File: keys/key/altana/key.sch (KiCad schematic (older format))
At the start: 13 parts

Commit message: Update
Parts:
- removed J? (x10): Conn_01x01_Female, Connector_Pin:Pin_D1.1mm_L8.5mm_W2.5mm_FlatFork, symbol Connector:Conn_01x01_Female
- added J1, J7: (+), kbd:wirepad-h0.8mm-d1.8mm, symbol Connector:Conn_01x01_Female
- added J10, J4: R, kbd:wirepad-h0.8mm-d1.8mm, symbol Connector:Conn_01x01_Female
- added J11, J5: DI, kbd:wirepad-h0.8mm-d1.8mm, symbol Connector:Conn_01x01_Female
- added J12, J6: DO, kbd:wirepad-h0.8mm-d1.8mm, symbol Connector:Conn_01x01_Female
- added J2, J8: (-), kbd:wirepad-h0.8mm-d1.8mm, symbol Connector:Conn_01x01_Female
- added J3, J9: C, kbd:wirepad-h0.8mm-d1.8mm, symbol Connector:Conn_01x01_Female
- D1: renamed from D?; footprint keebio_parts:Diode-Hybrid-Back -> footprint:diode
- gave numbers to parts that had none: 2
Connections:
- net GND: now also J2.1 (Pin_1), J8.1 (Pin_1)
- net VCC: now also J1.1 (Pin_1), J7.1 (Pin_1)
- net LED_DO: now reaches L1.1 (DOUT)
- net LED_DO: now also J12.1 (Pin_1), J6.1 (Pin_1)
- net LED_DI: now reaches L1.3 (DIN)
- net LED_DI: now also J11.1 (Pin_1), J5.1 (Pin_1)
- net COL renamed COL_N
- net COL_N: now also J3.1 (Pin_1), J9.1 (Pin_1)
- net ROW renamed ROW_N
- net ROW_N: now also J10.1 (Pin_1), J4.1 (Pin_1)
- no-connect marks 2 -> 0
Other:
- note added: "CONNECTORS"
- note added: "RGB LED"
- note added: "SWITCH"
- moved on the sheet: D1, L1, SW1

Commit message: Update project using kicad symbols whenever is possible and also update footprints to use project's library
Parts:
- removed L1: SK6812MINI, kbd:SK6812MINI_rev, symbol kbd:SK6812MINI
- added D2: SK6812MINI, Altana:SK6812MINI, symbol Altana:SK6812MINI
- D1: value D -> 1N4148; footprint footprint:diode -> Altana:diode
- J1, J10, J11, J12, J2, J3, J4, J5, J6, J7, J8, J9: footprint kbd:wirepad-h0.8mm-d1.8mm -> Altana:wirepad
- SW1: footprint kbd:MX_Hotswap_single -> Altana:Switch_MX_Hotswap
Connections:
- net GND: now also D2.2 (VSS)
- net LED_DI: now also D2.3 (DIN)
- net LED_DO: now also D2.1 (DOUT)
- net VCC: now also D2.4 (VDD)
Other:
- note removed: "CONNECTORS"
- note removed: "RGB LED"
- note removed: "SWITCH"
- moved on the sheet: D1
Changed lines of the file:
@@
 L Device:D D?
 U 1 1 5F6D17DD
-P 5300 3250
+P 5875 2875
 AR Path="/5F6D17DD" Ref="D?"  Part="1"
 AR Path="/5F6CE726/5F6D17DD" Ref="D1"  Part="1"
 AR Path="/5F6DC527/5F6D17DD" Ref="D?"  Part="1"
 AR Path="/5F6DC5E9/5F6D17DD" Ref="D?"  Part="1"
-F 0 "D1" H 5325 3050 50  0000 R CNN
-F 1 "D" H 5300 3150 50  0000 R CNN
-F 2 "footprint:diode" H 5300 3250 50  0001 C CNN
-F 3 "~" H 5300 3250 50  0001 C CNN
-	1    5300 3250
+F 0 "D1" H 5925 2650 50  0000 R CNN
+F 1 "1N4148" H 6025 2750 50  0000 R CNN
+F 2 "Altana:diode" H 5875 2875 50  0001 C CNN
+F 3 "~" H 5875 2875 50  0001 C CNN
+	1    5875 2875
 	-1   0    0    1
 $EndComp
-$Comp
-L kbd:SK6812MINI L?
-U 1 1 5F6D17E3
-P 6700 3150
-AR Path="/5F6D17E3" Ref="L?"  Part="1"
-AR Path="/5F6CE726/5F6D17E3" Ref="L1"  Part="1"
-AR Path="/5F6DC527/5F6D17E3" Ref="L?"  Part="1"
-AR Path="/5F6DC5E9/5F6D17E3" Ref="L?"  Part="1"
-F 0 "L1" H 6700 3350 51  0000 C CNN
-F 1 "SK6812MINI" H 6700 3150 16  0000 C CNN
-F 2 "kbd:SK6812MINI_rev" H 6700 3150 60  0001 C CNN
-F 3 "" H 6700 3150 60  0001 C CNN
-	1    6700 3150
-	-1   0    0    -1
-$EndComp
-$Comp
-L Switch:SW_Push SW?
-U 1 1 5F6D180E
-P 4900 3250
-AR Path="/5F6D180E" Ref="SW?"  Part="1"
-AR Path="/5F6CE726/5F6D180E" Ref="SW1"  Part="1"
-AR Path="/5F6DC527/5F6D180E" Ref="SW?"  Part="1"
-AR Path="/5F6DC5E9/5F6D180E" Ref="SW?"  Part="1"
-F 0 "SW1" H 4900 3535 50  0000 C CNN
-F 1 "SW_Push" H 4900 3444 50  0000 C CNN
-F 2 "kbd:MX_Hotswap_single" H 4900 3450 50  0001 C CNN
-F 3 "~" H 4900 3450 50  0001 C CNN
-	1    4900 3250
-	1    0    0    -1
-$EndComp
-Text HLabel 4600 3250 0    50   BiDi ~ 0
+Text HLabel 5150 2875 0    50   BiDi ~ 0
 COL_N
-Text HLabel 5500 3250 2    50   BiDi ~ 0
+Text HLabel 6075 2875 2    50   BiDi ~ 0
 ROW_N
 Wire Wire Line
-	5100 3250 5150 3250
-Wire Wire Line
-	5450 3250 5500 3250
-Wire Wire Line
-	4600 3250 4700 3250
-Wire Wire Line
-	6900 3250 6975 3250
-Text Notes 4700 2575 0    89   ~ 0
-SWITCH
-Text Notes 6450 2600 0    89   ~ 0
-RGB LED
+	5650 2875 5725 2875
+Wire Wire Line
+	6025 2875 6075 2875
+Wire Wire Line
+	5150 2875 5250 2875
+Wire Wire Line
+	5450 3450 5375 3450
 $Comp
 L Connector:Conn_01x01_Female J1
@@
 F 0 "J1" H 4953 4176 50  0000 L CNN
 F 1 "(+)" H 5100 4175 50  0000 L CNN
-F 2 "kbd:wirepad-h0.8mm-d1.8mm" H 4925 4150 50  0001 C CNN
+F 2 "Altana:wirepad" H 4925 4150 50  0001 C CNN
 F 3 "~" H 4925 4150 50  0001 C CNN
 	1    4925 4150
@@
 F 0 "J7" H 6578 4151 50  0000 L CNN
 F 1 "(+)" H 6578 4060 50  0000 L CNN
-F 2 "kbd:wirepad-h0.8mm-d1.8mm" H 6550 4125 50  0001 C CNN
+F 2 "Altana:wirepad" H 6550 4125 50  0001 C CNN
 F 3 "~" H 6550 4125 50  0001 C CNN
 	1    6550 4125
@@
 F 0 "J2" H 4953 4376 50  0000 L CNN
 F 1 "(-)" H 5100 4375 50  0000 L CNN
-F 2 "kbd:wirepad-h0.8mm-d1.8mm" H 4925 4350 50  0001 C CNN
+F 2 "Altana:wirepad" H 4925 4350 50  0001 C CNN
 F 3 "~" H 4925 4350 50  0001 C CNN
 	1    4925 4350
@@
 F 0 "J8" H 6578 4351 50  0000 L CNN
 F 1 "(-)" H 6578 4260 50  0000 L CNN
-F 2 "kbd:wirepad-h0.8mm-d1.8mm" H 6550 4325 50  0001 C CNN
+F 2 "Altana:wirepad" H 6550 4325 50  0001 C CNN
 F 3 "~" H 6550 4325 50  0001 C CNN
 	1    6550 4325
@@
 F 0 "J3" H 4953 4576 50  0000 L CNN
 F 1 "C" H 5100 4575 50  0000 L CNN
-F 2 "kbd:wirepad-h0.8mm-d1.8mm" H 4925 4550 50  0001 C CNN
+F 2 "Altana:wirepad" H 4925 4550 50  0001 C CNN
 F 3 "~" H 4925 4550 50  0001 C CNN
 	1    4925 4550
@@
 F 0 "J9" H 6578 4576 50  0000 L CNN
 F 1 "C" H 6578 4485 50  0000 L CNN
-F 2 "kbd:wirepad-h0.8mm-d1.8mm" H 6550 4550 50  0001 C CNN
+F 2 "Altana:wirepad" H 6550 4550 50  0001 C CNN
 F 3 "~" H 6550 4550 50  0001 C CNN
 	1    6550 4550
@@
 F 0 "J4" H 4953 4776 50  0000 L CNN
 F 1 "R" H 5100 4775 50  0000 L CNN
-F 2 "kbd:wirepad-h0.8mm-d1.8mm" H 4925 4750 50  0001 C CNN
+F 2 "Altana:wirepad" H 4925 4750 50  0001 C CNN
 F 3 "~" H 4925 4750 50  0001 C CNN
 	1    4925 4750
@@
 F 0 "J10" H 6578 4776 50  0000 L CNN
 F 1 "R" H 6578 4685 50  0000 L CNN
-F 2 "kbd:wirepad-h0.8mm-d1.8mm" H 6550 4750 50  0001 C CNN
+F 2 "Altana:wirepad" H 6550 4750 50  0001 C CNN
 F 3 "~" H 6550 4750 50  0001 C CNN
 	1    6550 4750
@@
 F 0 "J11" H 6578 4976 50  0000 L CNN
 F 1 "DI" H 6578 4885 50  0000 L CNN
-F 2 "kbd:wirepad-h0.8mm-d1.8mm" H 6550 4950 50  0001 C CNN
+F 2 "Altana:wirepad" H 6550 4950 50  0001 C CNN
 F 3 "~" H 6550 4950 50  0001 C CNN
 	1    6550 4950
@@
 F 0 "J12" H 6578 5176 50  0000 L CNN
 F 1 "DO" H 6578 5085 50  0000 L CNN
-F 2 "kbd:wirepad-h0.8mm-d1.8mm" H 6550 5150 50  0001 C CNN
+F 2 "Altana:wirepad" H 6550 5150 50  0001 C CNN
 F 3 "~" H 6550 5150 50  0001 C CNN
 	1    6550 5150
@@
 $EndComp
 Wire Wire Line
-	6400 3050 6500 3050
-Text HLabel 6400 3050 0    50   BiDi ~ 0
+	5950 3250 5850 3250
+Text HLabel 5950 3250 2    50   BiDi ~ 0
 VCC
-Text HLabel 6975 3250 2    50   BiDi ~ 0
+Text HLabel 5375 3450 0    50   BiDi ~ 0
 GND
 Text HLabel 4625 4150 0    50   BiDi ~ 0
@@
 Text HLabel 6250 4750 0    50   BiDi ~ 0
 ROW_N
-Text HLabel 6400 3250 0    50   BiDi ~ 0
+Text HLabel 5950 3450 2    50   BiDi ~ 0
 LED_DI
-Text HLabel 6975 3050 2    50   BiDi ~ 0
+Text HLabel 5375 3250 0    50   BiDi ~ 0
 LED_DO
 Wire Wire Line
-	6900 3050 6975 3050
-Wire Wire Line
-	6500 3250 6400 3250
+	5450 3250 5375 3250
+Wire Wire Line
+	5850 3450 5950 3450
 Text HLabel 4625 4950 0    50   BiDi ~ 0
 LED_DI
@@
 Wire Wire Line
 	4625 4150 4725 4150
-Text Notes 5625 3875 0    50   ~ 0
-CONNECTORS
 $Comp
 L Connector:Conn_01x01_Female J5
@@
 F 0 "J5" H 4953 4976 50  0000 L CNN
 F 1 "DI" H 5100 4975 50  0000 L CNN
-F 2 "kbd:wirepad-h0.8mm-d1.8mm" H 4925 4950 50  0001 C CNN
+F 2 "Altana:wirepad" H 4925 4950 50  0001 C CNN
 F 3 "~" H 4925 4950 50  0001 C CNN
 	1    4925 4950
@@
 F 0 "J6" H 4953 5176 50  0000 L CNN
 F 1 "DO" H 5100 5175 50  0000 L CNN
-F 2 "kbd:wirepad-h0.8mm-d1.8mm" H 4925 5150 50  0001 C CNN
+F 2 "Altana:wirepad" H 4925 5150 50  0001 C CNN
 F 3 "~" H 4925 5150 50  0001 C CNN
 	1    4925 5150
 	1    0    0    -1
 $EndComp
+$Comp
+L Switch:SW_Push SW1
+U 1 1 5F727337
+P 5450 2875
+F 0 "SW1" H 5450 3160 50  0000 C CNN
+F 1 "SW_Push" H 5450 3069 50  0000 C CNN
+F 2 "Altana:Switch_MX_Hotswap" H 5450 3075 50  0001 C CNN
+F 3 "~" H 5450 3075 50  0001 C CNN
+	1    5450 2875
+	1    0    0    -1
+$EndComp
+$Comp
+L Altana:SK6812MINI D2
+U 1 1 5F732BC5
+P 5650 3350
+F 0 "D2" H 5650 3575 51  0000 C CNN
+F 1 "SK6812MINI" H 5650 3350 28  0000 C CNN
+F 2 "Altana:SK6812MINI" H 5650 3350 60  0001 C CNN
+F 3 "https://cdn-shop.adafruit.com/product-files/2686/SK6812MINI_REV.01-1-2.pdf" H 5650 3350 60  0001 C CNN
+	1    5650 3350
+	1    0    0    -1
+$EndComp

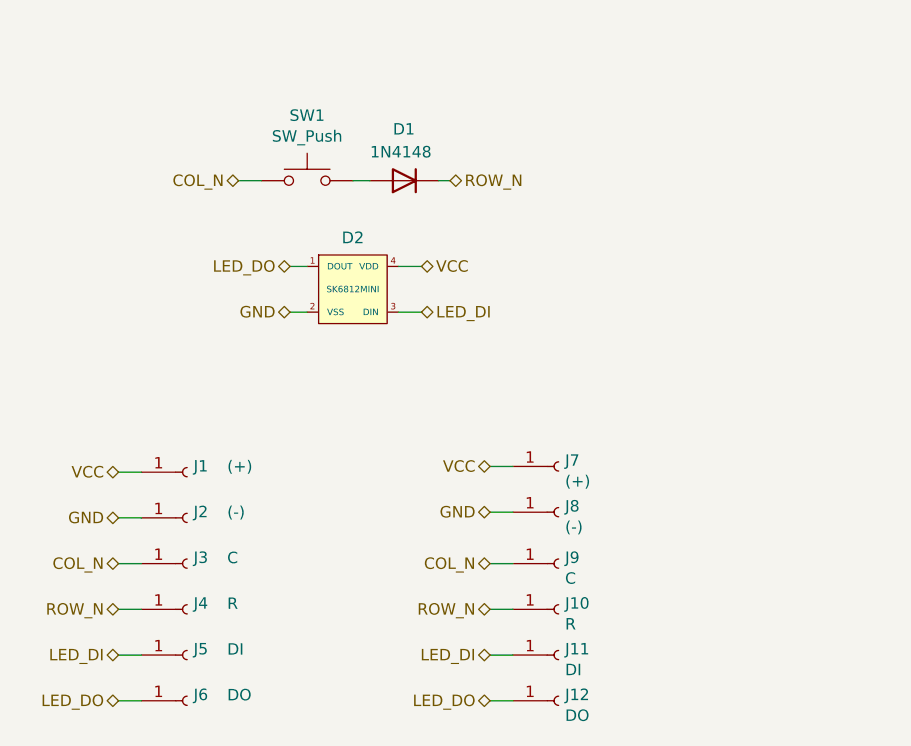
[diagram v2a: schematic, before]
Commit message: Add decoupling capacitor for the LED board
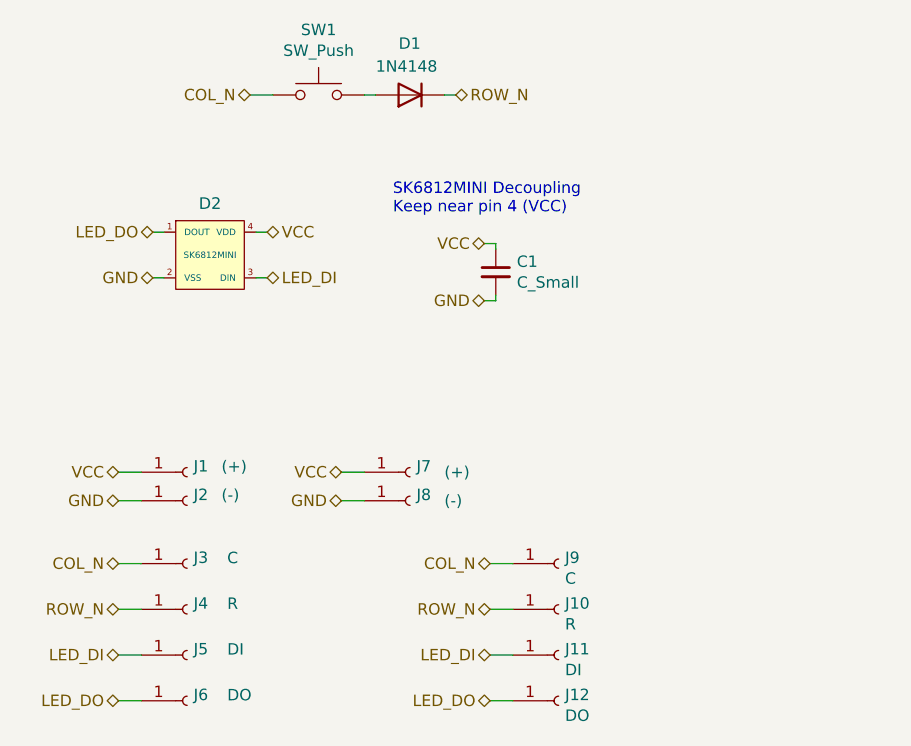
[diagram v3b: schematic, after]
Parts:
- added C1: C_Small, Capacitor_SMD:C_0805_2012Metric_Pad1.18x1.45mm_HandSolder, symbol Device:C_Small
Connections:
- net GND: now also C1.2
- net VCC: now also C1.1
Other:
- note added: "SK6812MINI Decoupling\nKeep near pin 4 (VCC)"
- moved on the sheet: D1, D2, J2, J7, J8, SW1
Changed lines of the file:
@@
 L Device:D D?
 U 1 1 5F6D17DD
-P 5875 2875
+P 5900 2500
 AR Path="/5F6D17DD" Ref="D?"  Part="1"
 AR Path="/5F6CE726/5F6D17DD" Ref="D1"  Part="1"
 AR Path="/5F6DC527/5F6D17DD" Ref="D?"  Part="1"
 AR Path="/5F6DC5E9/5F6D17DD" Ref="D?"  Part="1"
-F 0 "D1" H 5925 2650 50  0000 R CNN
-F 1 "1N4148" H 6025 2750 50  0000 R CNN
-F 2 "Altana:diode" H 5875 2875 50  0001 C CNN
-F 3 "~" H 5875 2875 50  0001 C CNN
-	1    5875 2875
+F 0 "D1" H 5950 2275 50  0000 R CNN
+F 1 "1N4148" H 6050 2375 50  0000 R CNN
+F 2 "Altana:diode" H 5900 2500 50  0001 C CNN
+F 3 "~" H 5900 2500 50  0001 C CNN
+	1    5900 2500
 	-1   0    0    1
 $EndComp
-Text HLabel 5150 2875 0    50   BiDi ~ 0
+Text HLabel 5200 2500 0    50   BiDi ~ 0
 COL_N
-Text HLabel 6075 2875 2    50   BiDi ~ 0
+Text HLabel 6100 2500 2    50   BiDi ~ 0
 ROW_N
 Wire Wire Line
-	5650 2875 5725 2875
-Wire Wire Line
-	6025 2875 6075 2875
-Wire Wire Line
-	5150 2875 5250 2875
-Wire Wire Line
-	5450 3450 5375 3450
+	5700 2500 5750 2500
+Wire Wire Line
+	6050 2500 6100 2500
+Wire Wire Line
+	5200 2500 5300 2500
+Wire Wire Line
+	4825 3300 4775 3300
 $Comp
 L Connector:Conn_01x01_Female J1
@@
 P 4925 4150
 F 0 "J1" H 4953 4176 50  0000 L CNN
-F 1 "(+)" H 5100 4175 50  0000 L CNN
+F 1 "(+)" H 5075 4175 50  0000 L CNN
 F 2 "Altana:wirepad" H 4925 4150 50  0001 C CNN
 F 3 "~" H 4925 4150 50  0001 C CNN
@@
 L Connector:Conn_01x01_Female J7
 U 1 1 5F70FDB4
-P 6550 4125
-F 0 "J7" H 6578 4151 50  0000 L CNN
-F 1 "(+)" H 6578 4060 50  0000 L CNN
-F 2 "Altana:wirepad" H 6550 4125 50  0001 C CNN
-F 3 "~" H 6550 4125 50  0001 C CNN
-	1    6550 4125
+P 5900 4150
+F 0 "J7" H 5928 4176 50  0000 L CNN
+F 1 "(+)" H 6050 4150 50  0000 L CNN
+F 2 "Altana:wirepad" H 5900 4150 50  0001 C CNN
+F 3 "~" H 5900 4150 50  0001 C CNN
+	1    5900 4150
 	1    0    0    -1
 $EndComp
@@
 L Connector:Conn_01x01_Female J2
 U 1 1 5F710812
-P 4925 4350
-F 0 "J2" H 4953 4376 50  0000 L CNN
-F 1 "(-)" H 5100 4375 50  0000 L CNN
-F 2 "Altana:wirepad" H 4925 4350 50  0001 C CNN
-F 3 "~" H 4925 4350 50  0001 C CNN
-	1    4925 4350
+P 4925 4275
+F 0 "J2" H 4953 4301 50  0000 L CNN
+F 1 "(-)" H 5075 4300 50  0000 L CNN
+F 2 "Altana:wirepad" H 4925 4275 50  0001 C CNN
+F 3 "~" H 4925 4275 50  0001 C CNN
+	1    4925 4275
 	1    0    0    -1
 $EndComp
@@
 L Connector:Conn_01x01_Female J8
 U 1 1 5F7112DE
-P 6550 4325
-F 0 "J8" H 6578 4351 50  0000 L CNN
-F 1 "(-)" H 6578 4260 50  0000 L CNN
-F 2 "Altana:wirepad" H 6550 4325 50  0001 C CNN
-F 3 "~" H 6550 4325 50  0001 C CNN
-	1    6550 4325
+P 5900 4275
+F 0 "J8" H 5928 4301 50  0000 L CNN
+F 1 "(-)" H 6050 4275 50  0000 L CNN
+F 2 "Altana:wirepad" H 5900 4275 50  0001 C CNN
+F 3 "~" H 5900 4275 50  0001 C CNN
+	1    5900 4275
 	1    0    0    -1
 $EndComp
@@
 	1    0    0    -1
 $EndComp
-Wire Wire Line
-	5950 3250 5850 3250
-Text HLabel 5950 3250 2    50   BiDi ~ 0
-VCC
-Text HLabel 5375 3450 0    50   BiDi ~ 0
+Text HLabel 4775 3300 0    50   BiDi ~ 0
 GND
 Text HLabel 4625 4150 0    50   BiDi ~ 0
 VCC
-Text HLabel 4625 4350 0    50   BiDi ~ 0
-GND
-Text HLabel 6250 4125 0    50   BiDi ~ 0
-VCC
-Text HLabel 6250 4325 0    50   BiDi ~ 0
+Text HLabel 4625 4275 0    50   BiDi ~ 0
+GND
+Text HLabel 5600 4150 0    50   BiDi ~ 0
+VCC
+Text HLabel 5600 4275 0    50   BiDi ~ 0
 GND
 Text HLabel 4625 4550 0    50   BiDi ~ 0
@@
 Text HLabel 6250 4750 0    50   BiDi ~ 0
 ROW_N
-Text HLabel 5950 3450 2    50   BiDi ~ 0
+Text HLabel 5275 3300 2    50   BiDi ~ 0
 LED_DI
-Text HLabel 5375 3250 0    50   BiDi ~ 0
+Text HLabel 4775 3100 0    50   BiDi ~ 0
 LED_DO
 Wire Wire Line
-	5450 3250 5375 3250
-Wire Wire Line
-	5850 3450 5950 3450
+	4825 3100 4775 3100
+Wire Wire Line
+	5225 3300 5275 3300
 Text HLabel 4625 4950 0    50   BiDi ~ 0
 LED_DI
@@
 	4625 4550 4725 4550
 Wire Wire Line
-	6250 4325 6350 4325
-Wire Wire Line
-	4625 4350 4725 4350
-Wire Wire Line
-	6250 4125 6350 4125
+	5600 4275 5700 4275
+Wire Wire Line
+	4625 4275 4725 4275
+Wire Wire Line
+	5600 4150 5700 4150
 Wire Wire Line
 	4625 4150 4725 4150
@@
 L Switch:SW_Push SW1
 U 1 1 5F727337
-P 5450 2875
-F 0 "SW1" H 5450 3160 50  0000 C CNN
-F 1 "SW_Push" H 5450 3069 50  0000 C CNN
-F 2 "Altana:Switch_MX_Hotswap" H 5450 3075 50  0001 C CNN
-F 3 "~" H 5450 3075 50  0001 C CNN
-	1    5450 2875
+P 5500 2500
+F 0 "SW1" H 5500 2785 50  0000 C CNN
+F 1 "SW_Push" H 5500 2694 50  0000 C CNN
+F 2 "Altana:Switch_MX_Hotswap" H 5500 2700 50  0001 C CNN
+F 3 "~" H 5500 2700 50  0001 C CNN
+	1    5500 2500
 	1    0    0    -1
 $EndComp
@@
 L Altana:SK6812MINI D2
 U 1 1 5F732BC5
-P 5650 3350
-F 0 "D2" H 5650 3575 51  0000 C CNN
-F 1 "SK6812MINI" H 5650 3350 28  0000 C CNN
-F 2 "Altana:SK6812MINI" H 5650 3350 60  0001 C CNN
-F 3 "https://cdn-shop.adafruit.com/product-files/2686/SK6812MINI_REV.01-1-2.pdf" H 5650 3350 60  0001 C CNN
-	1    5650 3350
-	1    0    0    -1
-$EndComp
+P 5025 3200
+F 0 "D2" H 5025 3425 51  0000 C CNN
+F 1 "SK6812MINI" H 5025 3200 28  0000 C CNN
+F 2 "Altana:SK6812MINI" H 5025 3200 60  0001 C CNN
+F 3 "https://cdn-shop.adafruit.com/product-files/2686/SK6812MINI_REV.01-1-2.pdf" H 5025 3200 60  0001 C CNN
+	1    5025 3200
+	1    0    0    -1
+$EndComp
+$Comp
+L Device:C_Small C1
+U 1 1 5F734A9A
+P 6275 3275
+F 0 "C1" H 6367 3321 50  0000 L CNN
+F 1 "C_Small" H 6367 3230 50  0000 L CNN
+F 2 "Capacitor_SMD:C_0805_2012Metric_Pad1.18x1.45mm_HandSolder" H 6275 3275 50  0001 C CNN
+F 3 "~" H 6275 3275 50  0001 C CNN
+	1    6275 3275
+	1    0    0    -1
+$EndComp
+Text HLabel 5275 3100 2    50   BiDi ~ 0
+VCC
+Wire Wire Line
+	5275 3100 5225 3100
+Text HLabel 6225 3150 0    50   BiDi ~ 0
+VCC
+Wire Wire Line
+	6275 3150 6275 3175
+Wire Wire Line
+	6225 3150 6275 3150
+Wire Wire Line
+	6275 3375 6275 3400
+Wire Wire Line
+	6275 3400 6225 3400
+Text HLabel 6225 3400 0    50   BiDi ~ 0
+GND
+Text Notes 5825 3025 0    50   ~ 0
+SK6812MINI Decoupling\nKeep near pin 4 (VCC)
 $EndSCHEMATC

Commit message: Update connections
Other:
- note added: "External Pins"
- moved on the sheet: C1, D1, D2, J1, J11, J12, J2, J3, J4, J5, J6, J7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
